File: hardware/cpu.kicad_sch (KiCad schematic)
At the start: 7 parts, among them U1 H3

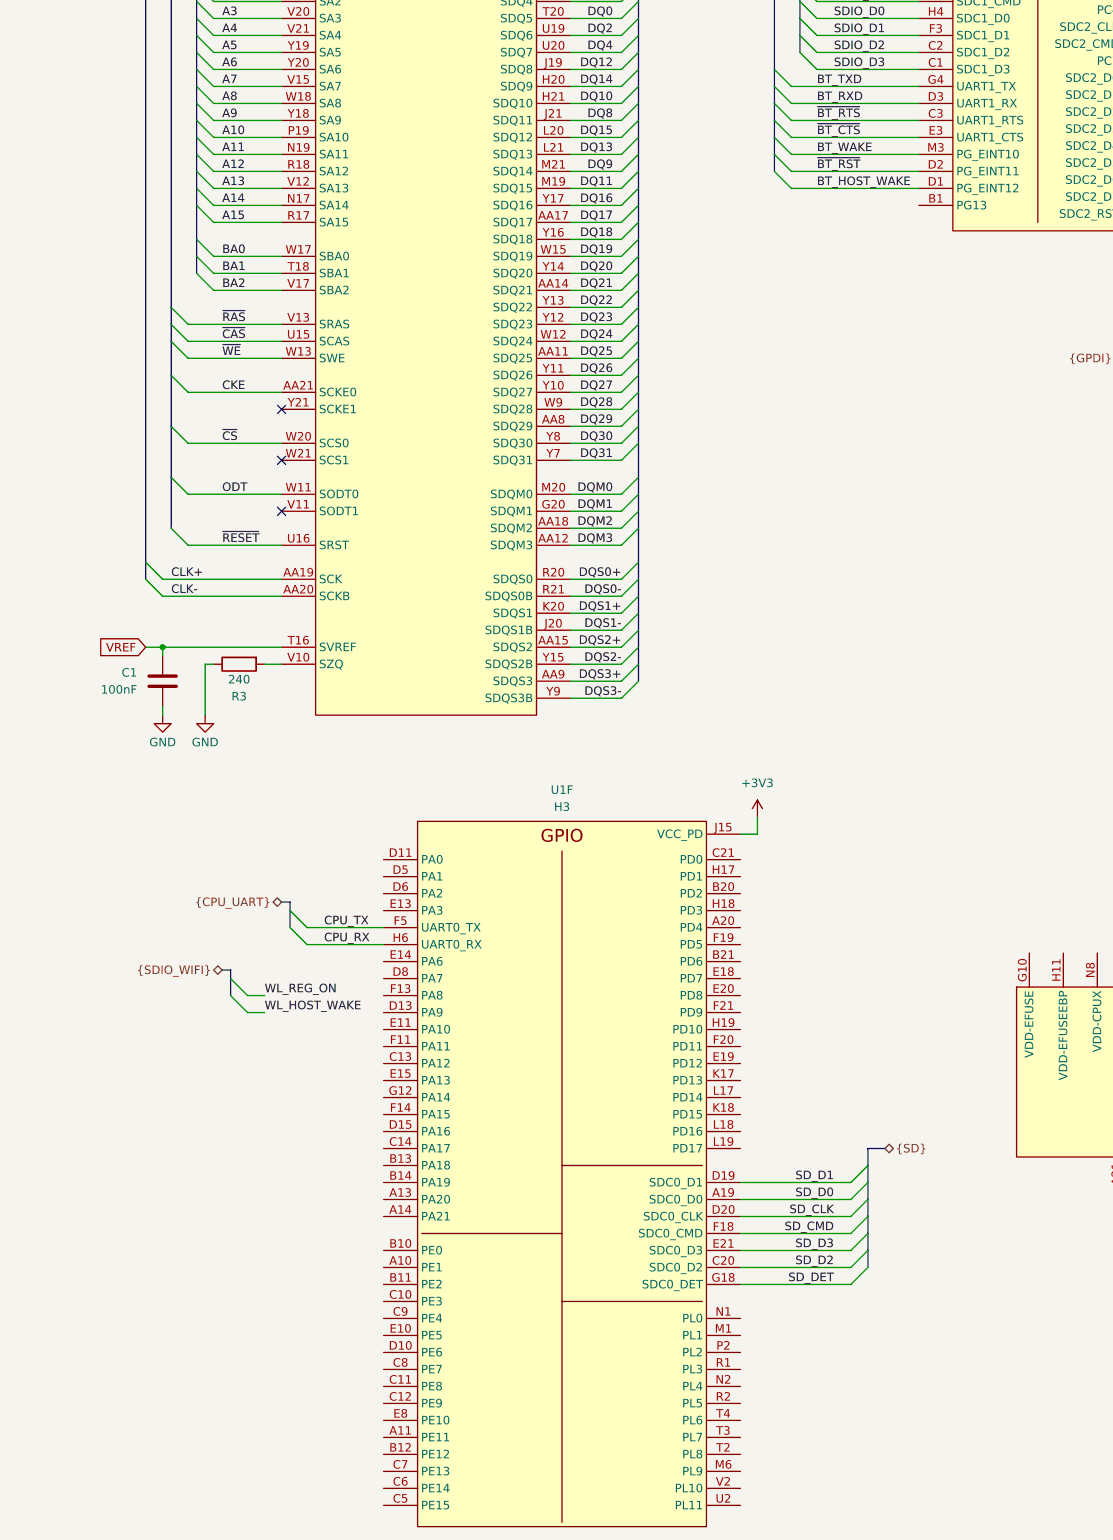
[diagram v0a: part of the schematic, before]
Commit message: Drew most of DC DC converters
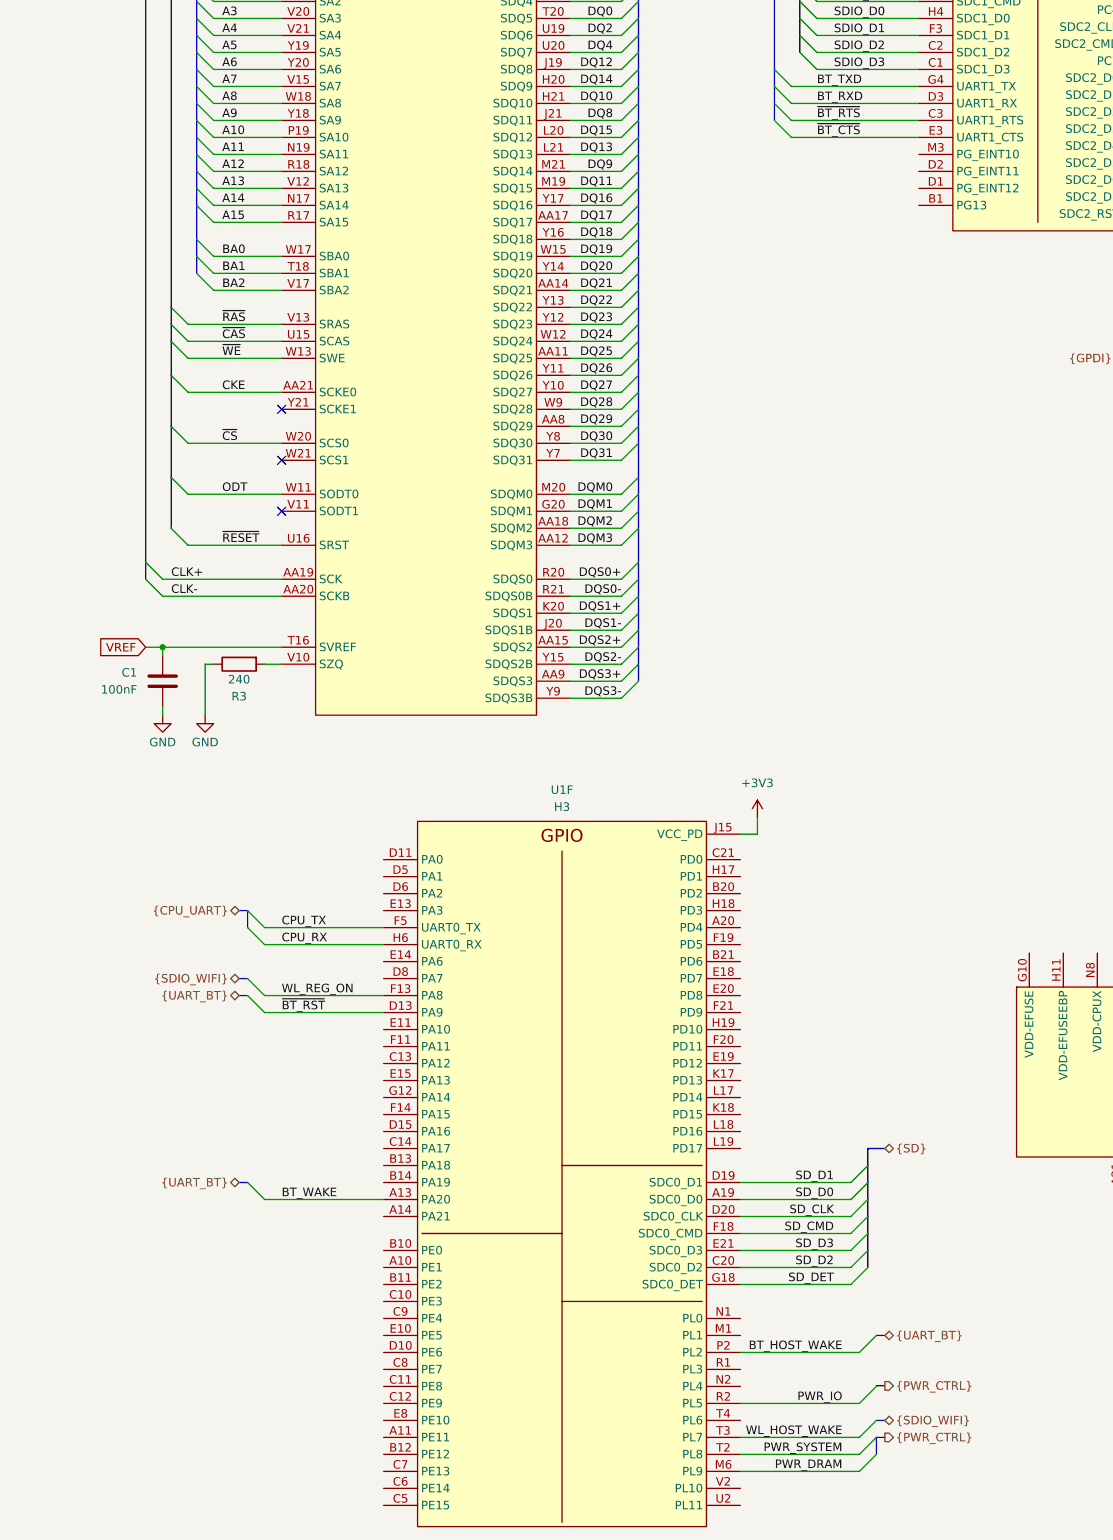
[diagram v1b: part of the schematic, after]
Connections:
- net BT_HOST_WAKE: now also U1.P2 (PL2); no longer U1.D1 (PG12)
- net BT_WAKE: now also U1.A13 (PA20); no longer U1.M3 (PG10)
- net WL_HOST_WAKE: now also U1.T3 (PL7)
- net WL_REG_ON: now also U1.F13 (PA8)
- net ~{BT_RST}: now also U1.D13 (PA9); no longer U1.D2 (PG11)
- net PWR_DRAM: now reaches U1.M6 (PL9)
- net PWR_IO: now reaches U1.R2 (PL5)
- net PWR_SYSTEM: now reaches U1.T2 (PL8)
